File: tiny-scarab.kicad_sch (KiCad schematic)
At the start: 40 parts, among them J2 TC2050-IDC-NL, J3 CONN_PIN_HEADER_02x07, J4 CONN_PIN_HEADER_02x07, J5 3mm, J6 3mm, J7 3mm, J8 3mm

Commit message: Schematic cleanup
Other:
- moved on the sheet: TVS10, TVS11, TVS12, TVS13, TVS14, TVS15, TVS16, TVS17, TVS18, TVS19, TVS20, TVS21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

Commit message: Apply JLCPCB rotations and offsets to components
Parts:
- J3, J4: JLCPCB Rotation Offset (none) -> 90

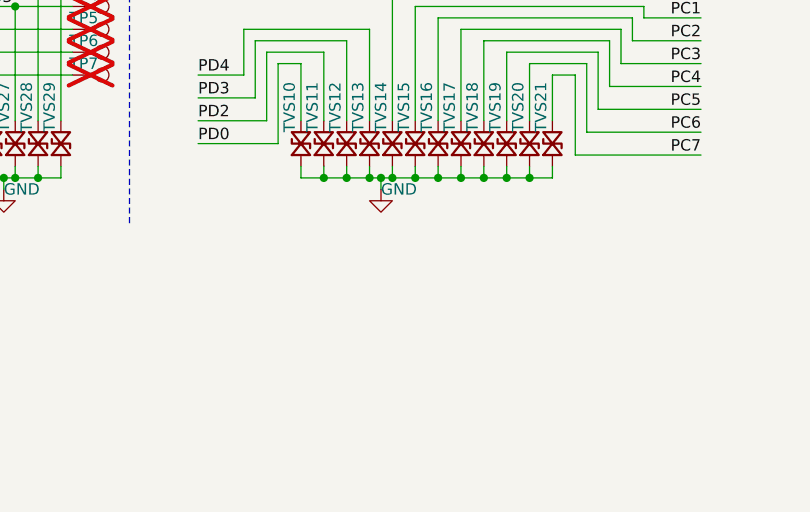
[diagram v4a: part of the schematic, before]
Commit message: Replace TVS `CDSOD323-T05LC` with `RLSD32A051LC`
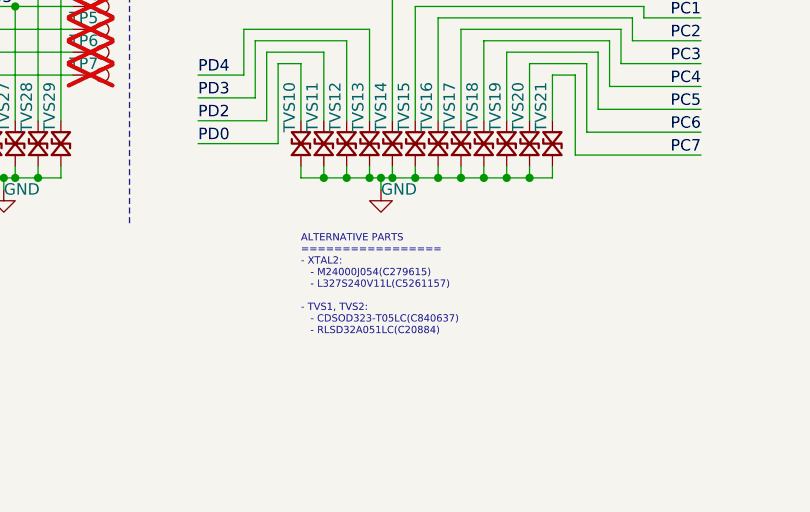
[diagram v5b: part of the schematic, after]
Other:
- note added: "ALTERNATIVE PARTS ================= - XTAL2: - M24000J054(C279615) - L327S240V11L(C5261157) - TVS1, TVS2: - CDSOD323-T05LC(C840637) - RLSD32A051LC(C20884)"
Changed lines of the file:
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@@
+		)
+	)
+	(text "ALTERNATIVE PARTS\n=================\n- XTAL2:\n   - M24000J054(C279615)\n   - L327S240V11L(C5261157)\n\n- TVS1, TVS2:\n   - CDSOD323-T05LC(C840637)\n   - RLSD32A051LC(C20884)"
+		(exclude_from_sim no)
+		(at 142.24 105.41 0)
+		(effects
+			(font
+				(size 0.8 0.8)
+			)
+			(justify left top)
 		)
 	)

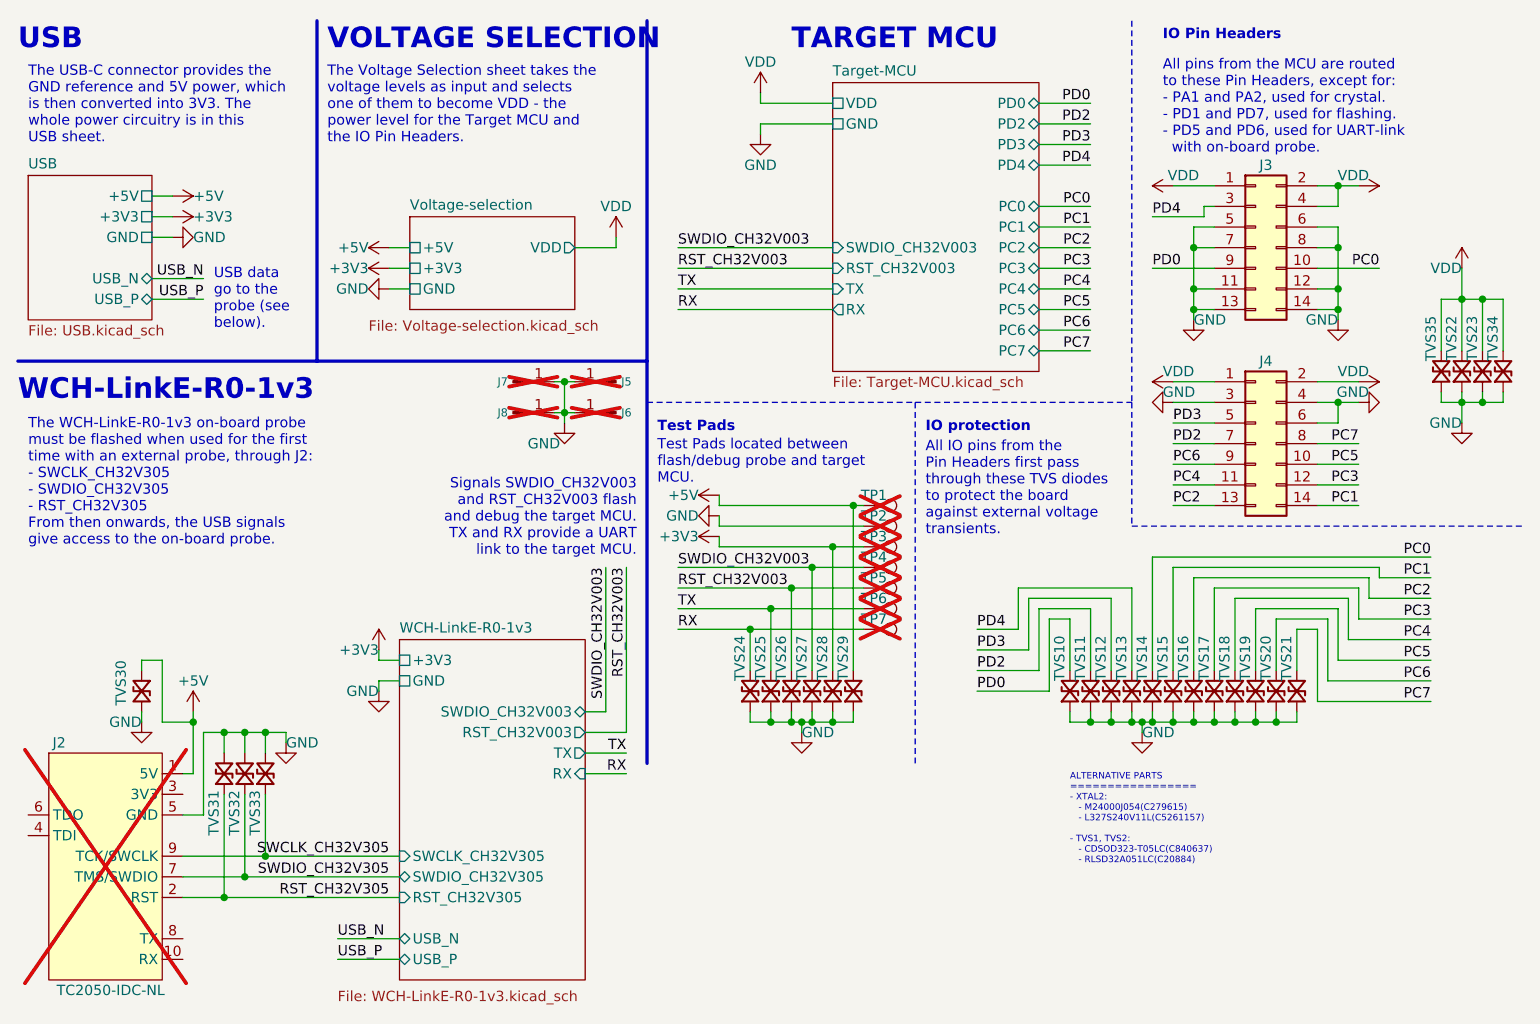
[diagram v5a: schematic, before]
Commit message: Replace TVS `SP1007-01ETG` with `LESD8LH5.0CT5G`
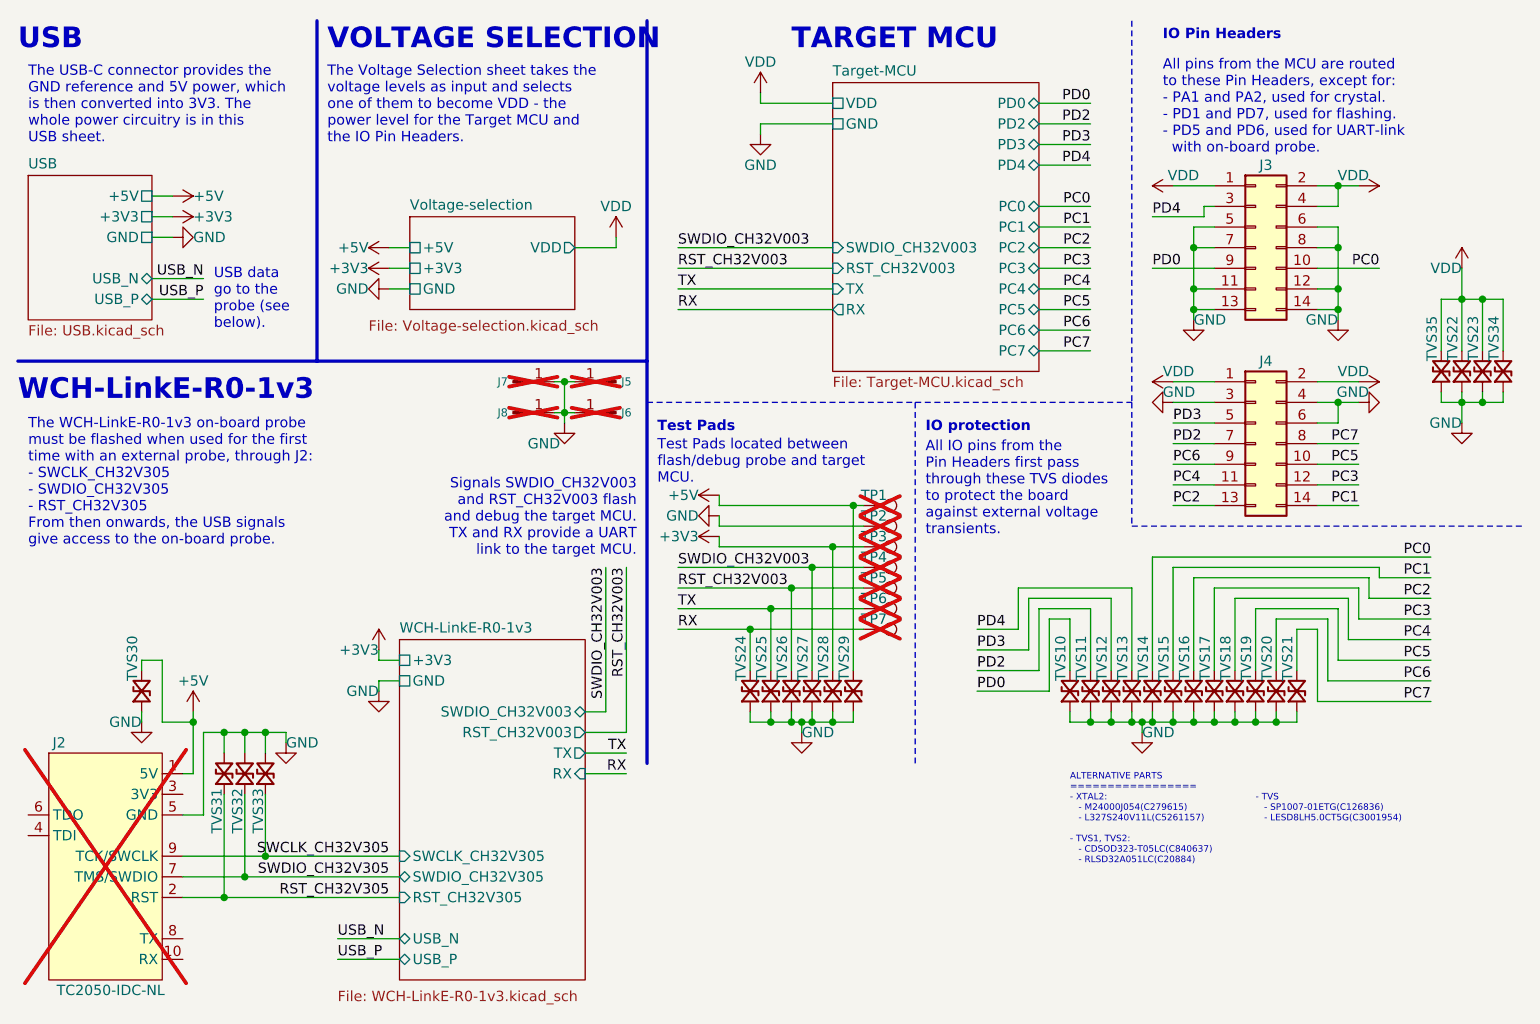
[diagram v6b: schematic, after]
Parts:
- removed TVS10, TVS11, TVS12, TVS13, TVS14, TVS15, TVS16, TVS17, TVS18, TVS19, TVS20, TVS21, TVS22, TVS23, TVS24, TVS25, TVS26, TVS27, TVS28, TVS29, TVS30, TVS31, TVS32, TVS33, TVS34, TVS35: 5V, Tiny_Scarab:D_SOD-882_SP1007-01ETG, symbol Tiny_Scarab:TVS_SP1007-01ETG
- added TVS10, TVS11, TVS12, TVS13, TVS14, TVS15, TVS16, TVS17, TVS18, TVS19, TVS20, TVS21, TVS22, TVS23, TVS24, TVS25, TVS26, TVS27, TVS28, TVS29, TVS30, TVS31, TVS32, TVS33, TVS34, TVS35: 5V, Tiny_Scarab:D_SOD-882_SP1007-01ETG, symbol Tiny_Scarab:TVS_LESD8LH5.0CT5G
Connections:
- net +3V3: now also TVS28.1
- net +5V: now also TVS29.1, TVS30.1
- net GND: now also TVS10.2, TVS11.2, TVS12.2, TVS13.2, TVS14.2, TVS15.2, TVS16.2, TVS17.2, TVS18.2, TVS19.2, TVS20.2, TVS21.2, TVS22.2, TVS23.2, TVS24.2, TVS25.2, TVS26.2, TVS27.2, TVS28.2, TVS29.2, TVS30.2, TVS31.1, TVS32.1, TVS33.1, TVS34.2, TVS35.2
- net PC0: now also TVS14.1
- net PC1: now also TVS15.1
- net PC2: now also TVS16.1
- net PC3: now also TVS17.1
- net PC4: now also TVS18.1
- net PC5: now also TVS19.1
- net PC6: now also TVS20.1
- net PC7: now also TVS21.1
- net PD0: now also TVS10.1
- net PD2: now also TVS11.1
- net PD3: now also TVS12.1
- net PD4: now also TVS13.1
- net RST_CH32V003: now also TVS26.1
- net RST_CH32V305: now also TVS31.2
- net RX: now also TVS24.1
- net SWCLK_CH32V305: now also TVS33.2
- net SWDIO_CH32V003: now also TVS27.1
- net SWDIO_CH32V305: now also TVS32.2
- net TX: now also TVS25.1
- net VDD: now also TVS22.1, TVS23.1, TVS34.1, TVS35.1
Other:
- note added: "- TVS - SP1007-01ETG(C126836) - LESD8LH5.0CT5G(C3001954)"
